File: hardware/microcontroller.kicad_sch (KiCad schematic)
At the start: 22 parts, among them J5 1x2 jumper right-angle, J6 Conn_02x03_Odd_Even, J7 1x2 jumper right-angle, U1 74LVC2G125, U15 74LVC138A, U17 74LVC138A

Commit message: Update header part numbers
SSW pins are incompatible with other headers.  SSQ should be better.  (Yet to confirm.)
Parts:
- J6: Mouser Part Number 200-SSW10301TD -> 200-SSQ10301TD; Part Number SSW-103-01-T-D -> SSQ-103-01-T-D
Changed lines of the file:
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@@
 			)
 		)
-		(property "Mouser Part Number" "200-SSW10301TD"
+		(property "Mouser Part Number" "200-SSQ10301TD"
 			(at 232.41 158.75 0)
 			(effects
@@
 			)
 		)
-		(property "Part Number" "SSW-103-01-T-D"
+		(property "Part Number" "SSQ-103-01-T-D"
 			(at 232.41 158.75 0)
 			(effects

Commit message: Drop Samtec headers
They do not connect well.  I need more reliable stacking headers.
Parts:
- J6: JLCPCB Part Number C6825448 -> C4944863; Mouser Part Number 200-SSQ10301TD -> 710-61300621821; Part Number SSQ-103-01-T-D -> 61300621821
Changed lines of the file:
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@@
 			)
 		)
-		(property "JLCPCB Part Number" "C6825448"
+		(property "JLCPCB Part Number" "C4944863"
 			(at 232.41 158.75 0)
 			(effects
@@
 			)
 		)
-		(property "Mouser Part Number" "200-SSQ10301TD"
+		(property "Mouser Part Number" "710-61300621821"
 			(at 232.41 158.75 0)
 			(effects
@@
 			)
 		)
-		(property "Part Number" "SSQ-103-01-T-D"
+		(property "Part Number" "61300621821"
 			(at 232.41 158.75 0)
 			(effects

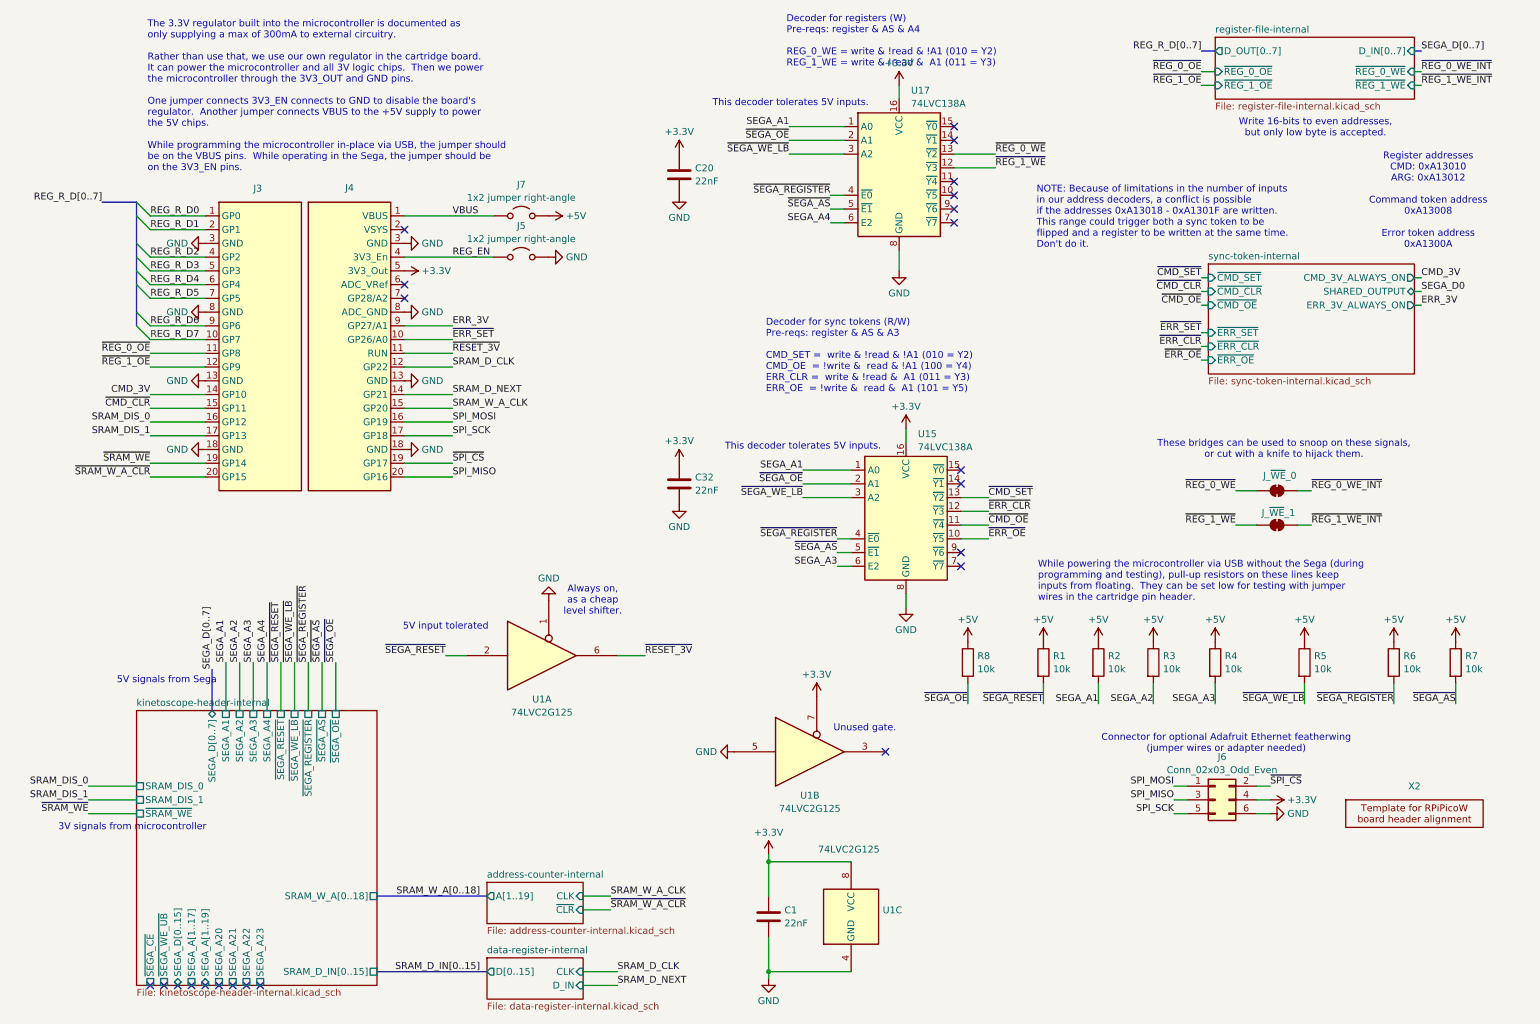
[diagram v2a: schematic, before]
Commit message: Remove reset line from Sega to uC
Also removes associated decoupler and pull-up resistor.

Closes #20
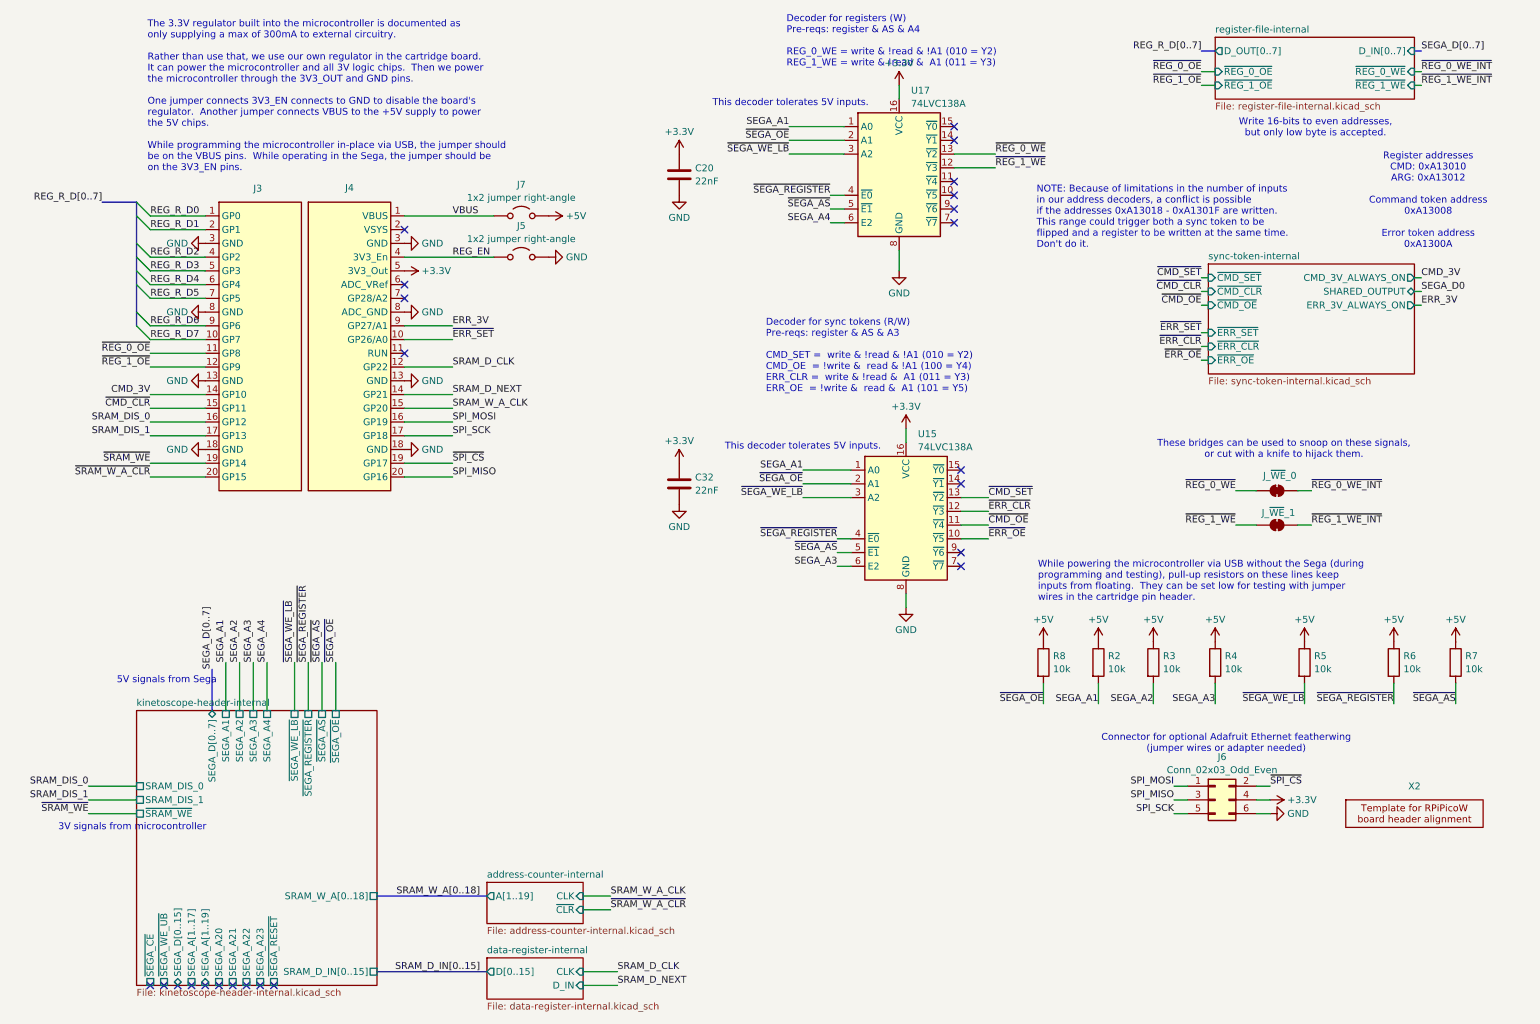
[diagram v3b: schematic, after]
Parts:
- removed C1: 22nF, Capacitor_SMD:C_0603_1608Metric, symbol Device:C
- removed R1: 10k, Resistor_SMD:R_0603_1608Metric, symbol Device:R
- removed U1: 74LVC2G125, Package_SO:VSSOP-8_2.3x2mm_P0.5mm, symbol 74xGxx:74LVC2G125
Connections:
- net ~{RESET_3V}: no longer names the net of J4.11 (RUN)
- no-connect marks 23 -> 24
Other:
- note removed: "5V input tolerated"
- note removed: "Always on, as a cheap level shifter."
- note removed: "Unused gate."
- moved on the sheet: R8
